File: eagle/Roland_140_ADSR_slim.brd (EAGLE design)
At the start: 98.7 x 45.7 mm, 61 parts, among them IC1 TL072P, Q1 BC557, Q2 BC557, Q3 BC557, T1 547, T10 547, T3 547, T4 547, T6 547, T7 547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

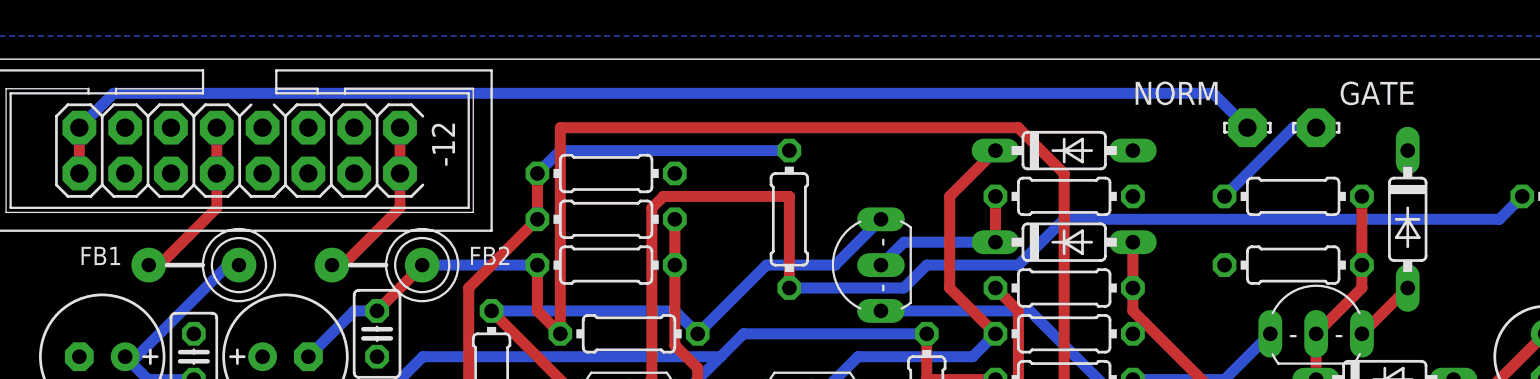
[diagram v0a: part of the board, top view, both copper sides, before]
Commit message: added ground for gate input
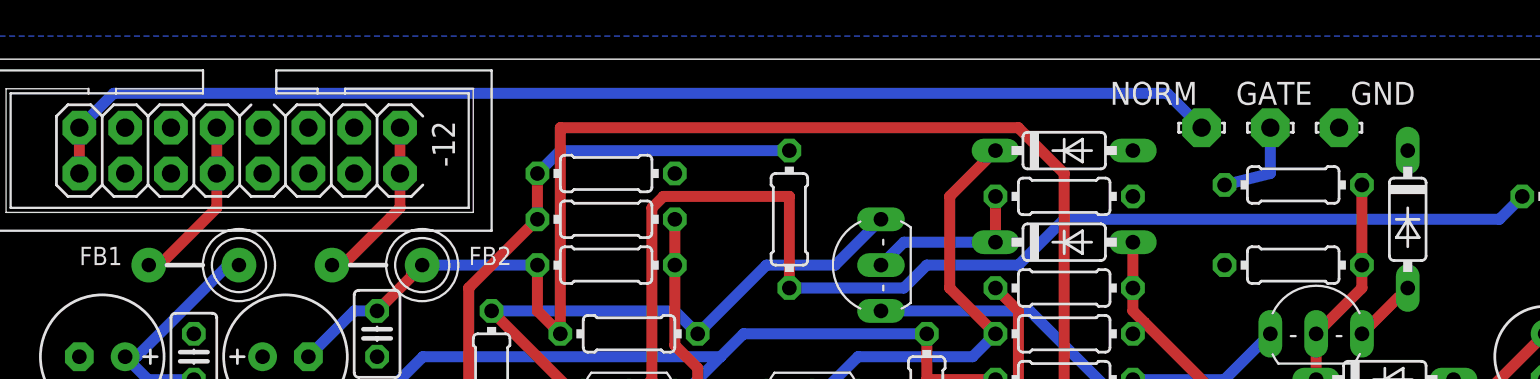
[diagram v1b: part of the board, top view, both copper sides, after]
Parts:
- added GND: LSP10, solpad:LSP10
- moved GATE 2.54 mm to (72.4, 41.9)
- moved NORM 2.54 mm to (68.6, 41.9)
- moved R3 0.63 mm to (73.7, 38.7)
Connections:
- net GND: now also GND.MP
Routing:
- net N$13: track 68.9 -> 66.3 mm
- net N$32: track 6.66 -> 5.16 mm
- net N$9: track 11.2 -> 11.8 mm
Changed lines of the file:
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@@
 <attribute name="VALUE" x="16.0274" y="11.7856" size="0.9906" layer="27" ratio="10" rot="R270"/>
 </element>
-<element name="R3" library="resistor" package="0204/7" value="33k" x="73.66" y="38.1" smashed="yes">
-<attribute name="SPICEPREFIX" value="R" x="73.66" y="38.1" size="1.778" layer="27" display="off"/>
-<attribute name="VALUE" x="72.0344" y="37.6174" size="0.9906" layer="27" ratio="10"/>
+<element name="R3" library="resistor" package="0204/7" value="33k" x="73.66" y="38.735" smashed="yes">
+<attribute name="SPICEPREFIX" value="R" x="73.66" y="38.735" size="1.778" layer="27" display="off"/>
+<attribute name="VALUE" x="72.0344" y="38.2524" size="0.9906" layer="27" ratio="10"/>
 </element>
 <element name="R4" library="resistor" package="0204/7" value="22k" x="73.66" y="34.29" smashed="yes">
@@
 <attribute name="VALUE" x="93.726" y="33.782" size="1.27" layer="27"/>
 </element>
-<element name="GATE" library="solpad" package="LSP10" value="LSP10" x="74.93" y="41.91" smashed="yes">
-<attribute name="NAME" x="76.2" y="43.18" size="1.27" layer="25" ratio="10"/>
-<attribute name="VALUE" x="74.93" y="42.164" size="0.0254" layer="27"/>
-</element>
-<element name="NORM" library="solpad" package="LSP10" value="LSP10" x="71.12" y="41.91" smashed="yes">
-<attribute name="NAME" x="64.77" y="43.18" size="1.27" layer="25" ratio="10"/>
-<attribute name="VALUE" x="71.12" y="42.164" size="0.0254" layer="27"/>
+<element name="GATE" library="solpad" package="LSP10" value="LSP10" x="72.39" y="41.91" smashed="yes">
+<attribute name="NAME" x="70.485" y="43.18" size="1.27" layer="25" ratio="10"/>
+<attribute name="VALUE" x="72.39" y="42.164" size="0.0254" layer="27"/>
+</element>
+<element name="NORM" library="solpad" package="LSP10" value="LSP10" x="68.58" y="41.91" smashed="yes">
+<attribute name="NAME" x="63.5" y="43.18" size="1.27" layer="25" ratio="10"/>
+<attribute name="VALUE" x="68.58" y="42.164" size="0.0254" layer="27"/>
+</element>
+<element name="GND" library="solpad" package="LSP10" value="LSP10" x="76.2" y="41.91" smashed="yes">
+<attribute name="NAME" x="76.835" y="43.18" size="1.27" layer="25" ratio="10"/>
+<attribute name="VALUE" x="76.2" y="42.164" size="0.0254" layer="27"/>
 </element>
 </elements>
@@
 <vertex x="-1.27" y="-1.27"/>
 </polygon>
+<contactref element="GND" pad="MP"/>
 </signal>
 <signal name="+12V">
@@
 <contactref element="D1" pad="C"/>
 <wire x1="74.93" y1="30.48" x2="74.93" y2="27.94" width="0.6096" layer="1"/>
-<wire x1="77.47" y1="38.1" x2="77.47" y2="34.29" width="0.6096" layer="1"/>
+<wire x1="77.47" y1="38.735" x2="77.47" y2="34.29" width="0.6096" layer="1"/>
 <wire x1="77.47" y1="33.02" x2="74.93" y2="30.48" width="0.6096" layer="1"/>
 <wire x1="77.47" y1="34.29" x2="77.47" y2="33.02" width="0.6096" layer="1"/>
@@
 <contactref element="R3" pad="1"/>
 <contactref element="GATE" pad="MP"/>
-<wire x1="73.66" y1="41.91" x2="69.85" y2="38.1" width="0.6096" layer="16"/>
-<wire x1="74.93" y1="41.91" x2="73.66" y2="41.91" width="0.6096" layer="16"/>
+<wire x1="72.39" y1="39.37" x2="69.85" y2="38.735" width="0.6096" layer="16"/>
+<wire x1="72.39" y1="41.91" x2="72.39" y2="39.37" width="0.6096" layer="16"/>
 </signal>
 <signal name="N$10">
@@
 <contactref element="NORM" pad="MP"/>
 <wire x1="6.35" y1="41.91" x2="6.35" y2="39.37" width="0.6096" layer="1"/>
-<wire x1="69.215" y1="43.815" x2="71.12" y2="41.91" width="0.6096" layer="16"/>
-<wire x1="8.255" y1="43.815" x2="69.215" y2="43.815" width="0.6096" layer="16"/>
+<wire x1="66.675" y1="43.815" x2="68.58" y2="41.91" width="0.6096" layer="16"/>
+<wire x1="8.255" y1="43.815" x2="66.675" y2="43.815" width="0.6096" layer="16"/>
 <wire x1="6.35" y1="41.91" x2="8.255" y2="43.815" width="0.6096" layer="16"/>
 </signal>

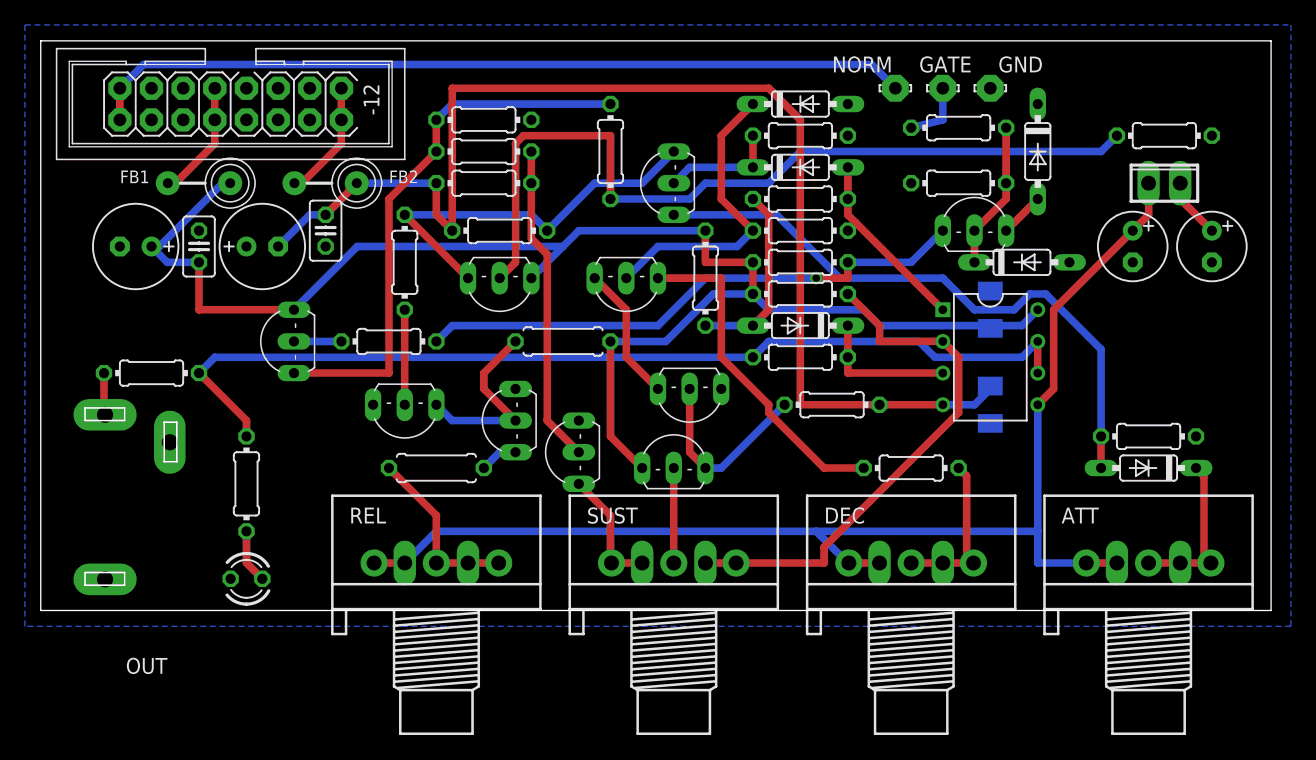
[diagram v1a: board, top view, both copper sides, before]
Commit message: slightly shorter for room for gate input
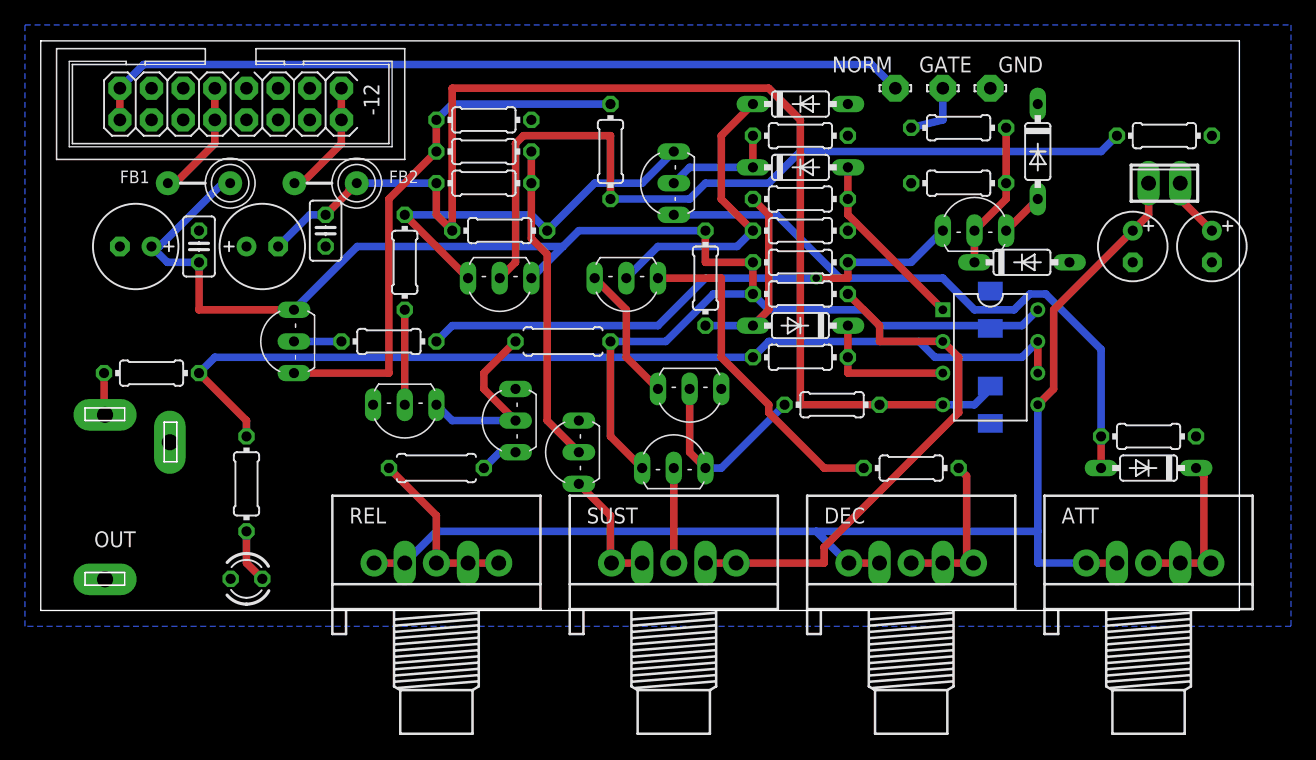
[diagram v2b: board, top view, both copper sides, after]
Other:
- board size 98.7 x 45.7 mm -> 96.2 x 45.7 mm
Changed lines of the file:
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@@
 <board>
 <plain>
-<wire x1="0" y1="0" x2="98.73" y2="0" width="0" layer="20"/>
-<wire x1="98.73" y1="0" x2="98.73" y2="45.71" width="0" layer="20"/>
-<wire x1="98.73" y1="45.71" x2="0" y2="45.71" width="0" layer="20"/>
+<wire x1="0" y1="0" x2="96.19" y2="0" width="0" layer="20"/>
+<wire x1="96.19" y1="0" x2="96.19" y2="45.71" width="0" layer="20"/>
+<wire x1="96.19" y1="45.71" x2="0" y2="45.71" width="0" layer="20"/>
 <wire x1="0" y1="45.71" x2="0" y2="0" width="0" layer="20"/>
-<text x="97.79" y="6.985" size="2.1844" layer="26" rot="MR0">https://github.com/jbeuckm/Roland-140-EG-2layer.git</text>
+<text x="95.25" y="6.985" size="2.1844" layer="26" rot="MR0">https://github.com/jbeuckm/Roland-140-EG-2layer.git</text>
 <text x="22.225" y="6.985" size="2.1844" layer="26" rot="MR0">Release v0.1</text>
 </plain>
@@
 <element name="ATT" library="pot" package="3RP/1610N" value="A500K" x="88.9" y="3.81" smashed="yes">
 <attribute name="NAME" x="81.915" y="6.985" size="1.27" layer="25"/>
-<attribute name="VALUE" x="92.075" y="6.35" size="1.27" layer="27"/>
+<attribute name="VALUE" x="89.535" y="7.62" size="1.27" layer="27"/>
 </element>
 <element name="C1" library="resistor" package="E2,5-7" value="47u" x="7.62" y="29.21" smashed="yes" rot="R180">
@@
 </element>
 <element name="OUT" library="erthenvar" package="JACK-90DEG-ITEAD" value="AUDIO-JACKITEAD" x="10.16" y="0" smashed="yes" rot="R180">
-<attribute name="NAME" x="10.16" y="-3.81" size="1.27" layer="21" rot="R180"/>
+<attribute name="NAME" x="7.62" y="6.35" size="1.27" layer="21" rot="R180"/>
 </element>
 <element name="Q1" library="transistor-pnp" package="TO92-EBC" value="BC557" x="19.05" y="21.59" smashed="yes" rot="R90">
